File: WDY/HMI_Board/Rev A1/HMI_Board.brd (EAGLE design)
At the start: 128 x 31.5 mm, 30 parts, among them SW1 B3FS-1015, SW2 B3FS-1015, SW3 B3FS-1015, SW4 B3FS-1015, SW5 B3FS-1015, SW6 B3FS-1015, U1 90814-0208, U2 90814-0206

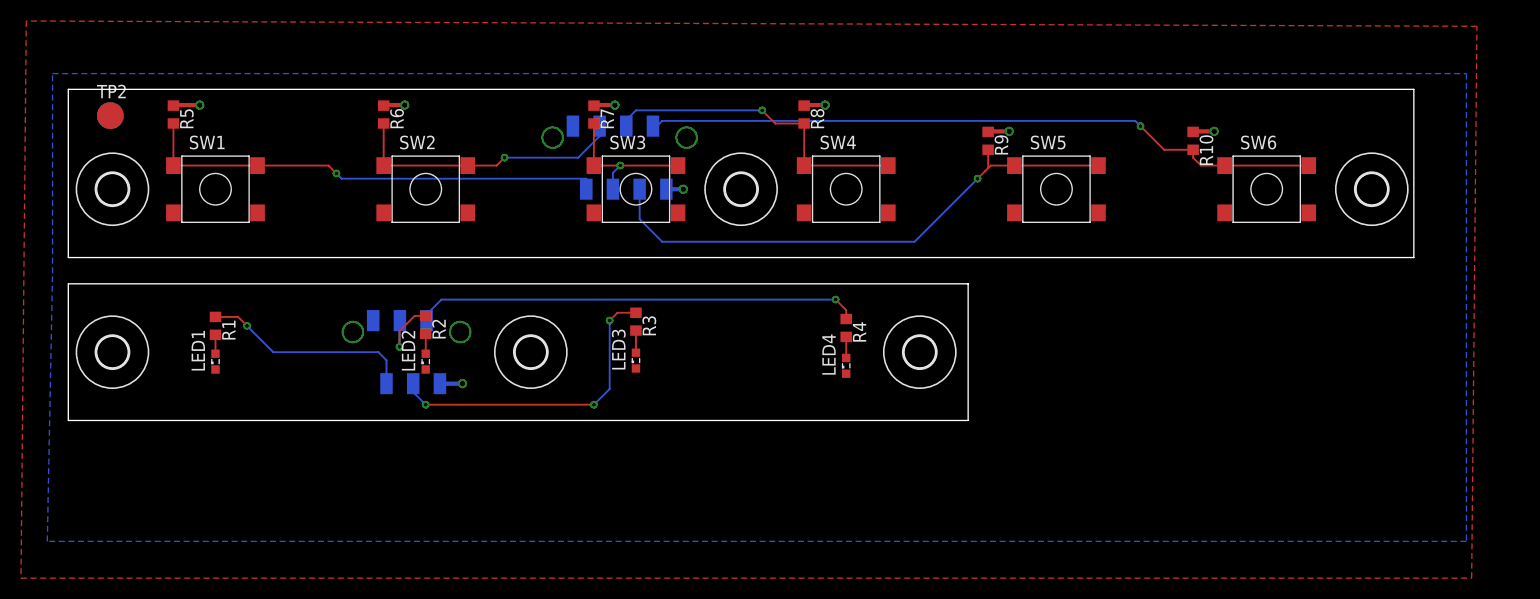
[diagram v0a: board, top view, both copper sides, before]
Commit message: Panelize the board, add fiducial
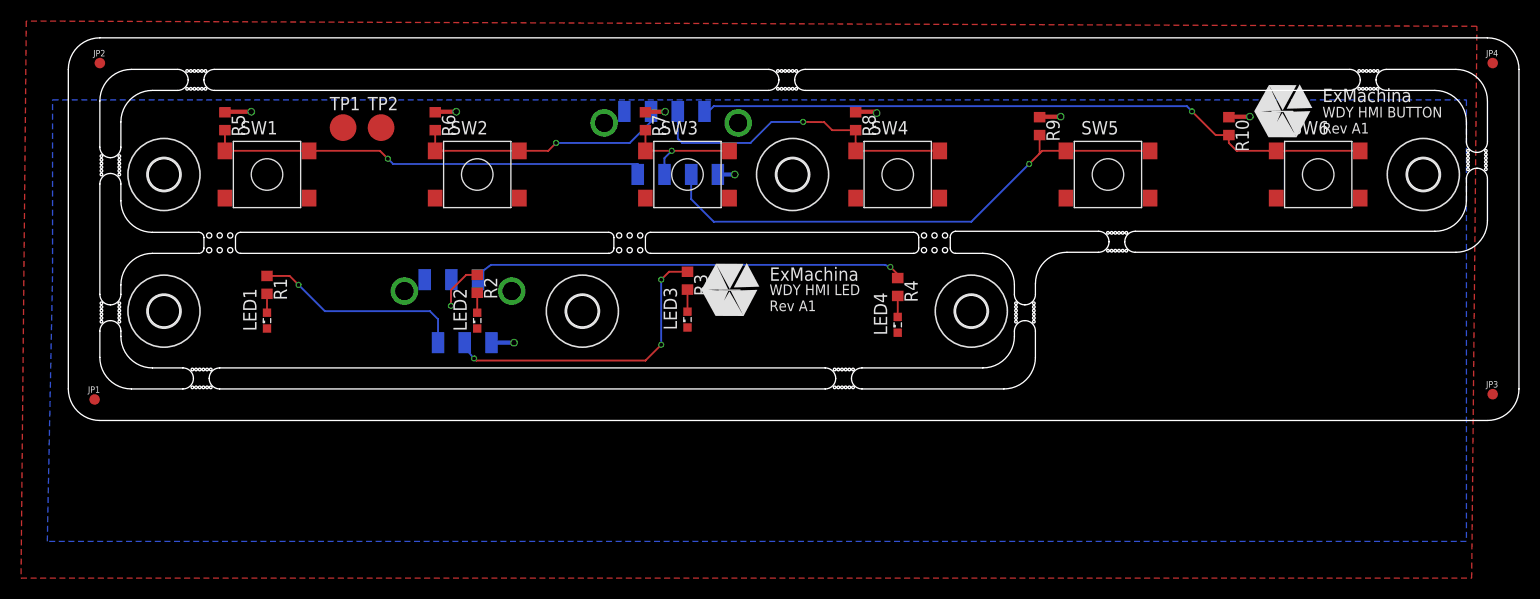
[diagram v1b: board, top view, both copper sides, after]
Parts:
- added JP1, JP2, JP3, JP4: FIDUCIAL1X2, SparkFun:FIDUCIAL-1X2
- added U$1, U$2: EXMACHINA-LOGO-NAME, exmachina:EXM-LOGO-BASELINE
- moved TP2 25.8 mm to (29.8, 27.9)
- moved TP1 22.2 mm to (26.1, 27.9), flipped to the top
- moved H4 6.26 mm to (85.9, 10.4)
- moved LED4 6.26 mm to (78.9, 9.10)
- moved R4 6.26 mm to (78.9, 12.7)
- moved H3 6.26 mm to (9.10, 10.4)
- moved H5 6.26 mm to (48.9, 10.4)
- moved LED1 6.26 mm to (18.9, 9.50)
- moved LED2 6.26 mm to (38.9, 9.50)
- moved R1 6.26 mm to (18.9, 12.9)
- moved R2 6.26 mm to (38.9, 13.0)
- moved R3 6.26 mm to (58.9, 13.3)
- moved U2 6.26 mm to (33.9, 13.4)
- moved LED3 6.26 mm to (58.9, 9.60)
- moved H1 5.10 mm to (128.9, 23.4)
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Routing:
- net HMI_BUTTON_2: track 26.7 -> 24.6 mm
- net HMI_BUTTON_1: track 44.8 -> 42.7 mm
- net HMI_BUTTON_3: track 14.5 -> 12.5 mm
- net HMI_BUTTON_4: track 30.4 -> 31.4 mm
- net HMI_LED_4: track 42.4 -> 41.4 mm
- net HMI_BUTTON_5: track 52.1 -> 51.4 mm
- net HMI_LED_3: track 29.9 -> 29.4 mm
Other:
- board size 128 x 31.5 mm -> 138 x 36.4 mm
- board text added: "WDY HMI BUTTON Rev A1"
- board text added: "WDY HMI LED Rev A1"

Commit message: Update libraries
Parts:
- moved TP2 6.48 mm to (23.4, 28.9)
- moved TP1 6.18 mm to (20.0, 28.9)
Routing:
- net +3V3: track 12.5 -> 15.7 mm
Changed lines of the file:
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@@
 <element name="H5" library="holes" package="3,0" value="MOUNT-HOLE3.0" x="48.9" y="10.4"/>
 <element name="H6" library="holes" package="3,0" value="MOUNT-HOLE3.0" x="9.1" y="23.4"/>
-<element name="TP1" library="testpad" package="B2,54" value="TPB2,54" x="26.14" y="27.86">
-<attribute name="TP_SIGNAL_NAME" value="" x="26.14" y="27.86" size="1.778" layer="27" display="off"/>
+<element name="TP1" library="testpad" package="B2,54" value="TPB2,54" x="20.04" y="28.86">
+<attribute name="TP_SIGNAL_NAME" value="" x="20.04" y="28.86" size="1.778" layer="27" display="off"/>
 </element>
-<element name="TP2" library="testpad" package="B2,54" value="TPB2,54" x="29.752" y="27.86">
-<attribute name="TP_SIGNAL_NAME" value="" x="29.752" y="27.86" size="1.778" layer="27" display="off"/>
+<element name="TP2" library="testpad" package="B2,54" value="TPB2,54" x="23.352" y="28.86">
+<attribute name="TP_SIGNAL_NAME" value="" x="23.352" y="28.86" size="1.778" layer="27" display="off"/>
 </element>
 <element name="U$1" library="exmachina" package="EXM-LOGO-BASELINE" value="EXMACHINA-LOGO-NAME" x="62.9" y="12.4"/>
@@
 <wire x1="40.2556" y1="7.4" x2="42.4" y2="7.4" width="0.4064" layer="16"/>
 <via x="42.4" y="7.4" extent="1-16" drill="0.5"/>
-<wire x1="58.9" y1="8.85" x2="54.9" y2="21.15" width="0" layer="19" extent="1-1"/>
+<wire x1="54.9" y1="21.15" x2="58.9" y2="8.85" width="0" layer="19" extent="1-1"/>
 </signal>
 <signal name="+3V3">
@@
 <wire x1="74.95" y1="29.368" x2="76.773" y2="29.368" width="0.4064" layer="1"/>
 <wire x1="76.773" y1="29.368" x2="76.9" y2="29.241" width="0.4064" layer="1"/>
-<wire x1="17.4" y1="29.368" x2="26.14" y2="27.86" width="0" layer="19" extent="1-1"/>
-<wire x1="52.9" y1="29.4" x2="54.9" y2="29.318" width="0" layer="19" extent="1-16"/>
-<wire x1="33.9" y1="13.4" x2="34.9" y2="29.318" width="0" layer="19" extent="1-16"/>
+<wire x1="17.4" y1="29.368" x2="20.04" y2="29.368" width="0.4064" layer="1"/>
+<wire x1="20.04" y1="29.368" x2="20.04" y2="28.86" width="0.4064" layer="1"/>
+<wire x1="34.9" y1="29.318" x2="33.9" y2="13.4" width="0" layer="19" extent="1-16"/>
 </signal>
 <signal name="HMI_LED_1" class="1">
@@
 <wire x1="34.9" y1="25.65" x2="34.9" y2="27.618" width="0.1778" layer="1"/>
 <wire x1="42.9" y1="25.65" x2="34.9" y2="25.65" width="0.1778" layer="1"/>
-<wire x1="42.9" y1="25.65" x2="45.65" y2="25.65" width="0.1778" layer="1"/>
-<wire x1="45.65" y1="25.65" x2="46.4" y2="26.4" width="0.1778" layer="1"/>
-<via x="46.4" y="26.4" extent="1-16" drill="0.35"/>
-<wire x1="46.4" y1="26.4" x2="53.4" y2="26.4" width="0.1778" layer="16"/>
-<wire x1="53.4" y1="26.4" x2="55.44" y2="28.44" width="0.1778" layer="16"/>
+<wire x1="42.9" y1="25.65" x2="46.15" y2="25.65" width="0.1778" layer="1"/>
+<wire x1="46.15" y1="25.65" x2="46.4" y2="25.9" width="0.1778" layer="1"/>
+<via x="46.4" y="25.9" extent="1-16" drill="0.35"/>
+<wire x1="46.4" y1="25.9" x2="52.9" y2="25.9" width="0.1778" layer="16"/>
+<wire x1="52.9" y1="25.9" x2="55.44" y2="28.44" width="0.1778" layer="16"/>
 <wire x1="55.44" y1="28.44" x2="55.44" y2="29.4" width="0.1778" layer="16"/>
 </signal>

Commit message: Add value on LED
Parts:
- LED1, LED2, LED3, LED4: value (none) -> Blue
- moved U1 5.41 mm to (57.4, 26.4)
- moved U2 3.91 mm to (36.9, 10.9)
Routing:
- net GND: track 3.76 -> 4.64 mm
- net HMI_LED_2: track 7.12 -> 7.79 mm
- net HMI_LED_3: track 29.4 -> 30.0 mm
- net HMI_LED_1: track 20.2 -> 19.5 mm
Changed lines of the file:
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@@
 </autorouter>
 <elements>
-<element name="LED1" library="led" package="SML0603" value="" x="18.9" y="9.5" rot="R90"/>
-<element name="LED2" library="led" package="SML0603" value="" x="38.9" y="9.5" rot="R90"/>
-<element name="LED3" library="led" package="SML0603" value="" x="58.9" y="9.6" rot="R90"/>
-<element name="LED4" library="led" package="SML0603" value="" x="78.9" y="9.1" rot="R90"/>
+<element name="LED1" library="led" package="SML0603" value="Blue" x="18.9" y="9.5" rot="R90"/>
+<element name="LED2" library="led" package="SML0603" value="Blue" x="38.9" y="9.5" rot="R90"/>
+<element name="LED3" library="led" package="SML0603" value="Blue" x="58.9" y="9.6" rot="R90"/>
+<element name="LED4" library="led" package="SML0603" value="Blue" x="78.9" y="9.1" rot="R90"/>
 <element name="R1" library="rcl" package="R0603" value="1k" x="18.9" y="12.9" rot="R270"/>
 <element name="R2" library="rcl" package="R0603" value="1k" x="38.9" y="13" rot="R270"/>
@@
 <element name="SW5" library="Switch_SMT" package="B3FS" value="B3FS-1015" x="98.9" y="23.4"/>
 <element name="R9" library="rcl" package="R0603" value="4k7" x="92.4" y="28" rot="R270"/>
-<element name="U1" library="Molex_By_element14_Batch_1" package="MOLEX_90814-0208" value="90814-0208" x="52.9" y="29.4" rot="MR180">
-<attribute name="SUPPLIER" value="Molex" x="52.9" y="29.4" size="1.778" layer="28" rot="MR180" display="off"/>
-<attribute name="MPN" value="90814-0208" x="52.9" y="29.4" size="1.778" layer="28" rot="MR180" display="off"/>
-<attribute name="OC_FARNELL" value="1757025" x="52.9" y="29.4" size="1.778" layer="28" rot="MR180" display="off"/>
-<attribute name="OC_NEWARK" value="34R6216" x="52.9" y="29.4" size="1.778" layer="28" rot="MR180" display="off"/>
-<attribute name="PACKAGE" value="CONN-8POS" x="52.9" y="29.4" size="1.778" layer="28" rot="MR180" display="off"/>
+<element name="U1" library="Molex_By_element14_Batch_1" package="MOLEX_90814-0208" value="90814-0208" x="57.4" y="26.4" rot="MR180">
+<attribute name="SUPPLIER" value="Molex" x="57.4" y="26.4" size="1.778" layer="28" rot="MR180" display="off"/>
+<attribute name="MPN" value="90814-0208" x="57.4" y="26.4" size="1.778" layer="28" rot="MR180" display="off"/>
+<attribute name="OC_FARNELL" value="1757025" x="57.4" y="26.4" size="1.778" layer="28" rot="MR180" display="off"/>
+<attribute name="OC_NEWARK" value="34R6216" x="57.4" y="26.4" size="1.778" layer="28" rot="MR180" display="off"/>
+<attribute name="PACKAGE" value="CONN-8POS" x="57.4" y="26.4" size="1.778" layer="28" rot="MR180" display="off"/>
 </element>
 <element name="SW6" library="Switch_SMT" package="B3FS" value="B3FS-1015" x="118.9" y="23.4"/>
 <element name="R10" library="rcl" package="R0603" value="4k7" x="110.4" y="28" rot="R270"/>
-<element name="U2" library="Molex_By_element14_Batch_1" package="MOLEX_90814-0206" value="90814-0206" x="33.9" y="13.4" rot="MR180">
-<attribute name="SUPPLIER" value="Molex" x="33.9" y="13.4" size="1.778" layer="28" rot="MR180" display="off"/>
-<attribute name="MPN" value="90814-0206" x="33.9" y="13.4" size="1.778" layer="28" rot="MR180" display="off"/>
-<attribute name="OC_FARNELL" value="1757024" x="33.9" y="13.4" size="1.778" layer="28" rot="MR180" display="off"/>
-<attribute name="OC_NEWARK" value="34R6215" x="33.9" y="13.4" size="1.778" layer="28" rot="MR180" display="off"/>
-<attribute name="PACKAGE" value="CONN-6 POS" x="33.9" y="13.4" size="1.778" layer="28" rot="MR180" display="off"/>
+<element name="U2" library="Molex_By_element14_Batch_1" package="MOLEX_90814-0206" value="90814-0206" x="36.9" y="10.9" rot="MR180">
+<attribute name="SUPPLIER" value="Molex" x="36.9" y="10.9" size="1.778" layer="28" rot="MR180" display="off"/>
+<attribute name="MPN" value="90814-0206" x="36.9" y="10.9" size="1.778" layer="28" rot="MR180" display="off"/>
+<attribute name="OC_FARNELL" value="1757024" x="36.9" y="10.9" size="1.778" layer="28" rot="MR180" display="off"/>
+<attribute name="OC_NEWARK" value="34R6215" x="36.9" y="10.9" size="1.778" layer="28" rot="MR180" display="off"/>
+<attribute name="PACKAGE" value="CONN-6 POS" x="36.9" y="10.9" size="1.778" layer="28" rot="MR180" display="off"/>
 </element>
 <element name="H1" library="holes" package="3,0" value="MOUNT-HOLE3.0" x="128.9" y="23.4"/>
@@
 <vertex x="133.5" y="-15"/>
 </polygon>
-<wire x1="61.79" y1="23.4056" x2="61.7956" y2="23.4" width="0.4064" layer="16"/>
+<wire x1="61.845" y1="23.5806" x2="61.7956" y2="23.4" width="0.4064" layer="16"/>
 <wire x1="61.7956" y1="23.4" x2="63.4" y2="23.4" width="0.4064" layer="16"/>
 <via x="63.4" y="23.4" extent="1-16" drill="0.5"/>
 <contactref element="TP2" pad="TP"/>
-<wire x1="40.25" y1="7.4056" x2="40.2556" y2="7.4" width="0.4064" layer="16"/>
+<wire x1="40.075" y1="8.0806" x2="40.2556" y2="7.4" width="0.4064" layer="16"/>
 <wire x1="40.2556" y1="7.4" x2="42.4" y2="7.4" width="0.4064" layer="16"/>
 <via x="42.4" y="7.4" extent="1-16" drill="0.5"/>
-<wire x1="54.9" y1="21.15" x2="58.9" y2="8.85" width="0" layer="19" extent="1-1"/>
+<wire x1="58.9" y1="8.85" x2="54.9" y2="21.15" width="0" layer="19" extent="1-1"/>
 </signal>
 <signal name="+3V3">
@@
 <wire x1="17.4" y1="29.368" x2="20.04" y2="29.368" width="0.4064" layer="1"/>
 <wire x1="20.04" y1="29.368" x2="20.04" y2="28.86" width="0.4064" layer="1"/>
-<wire x1="34.9" y1="29.318" x2="33.9" y2="13.4" width="0" layer="19" extent="1-16"/>
+<wire x1="33.725" y1="14.075" x2="34.9" y2="29.318" width="0" layer="19" extent="1-16"/>
 </signal>
 <signal name="HMI_LED_1" class="1">
@@
 <wire x1="24.4" y1="10.4" x2="34.4" y2="10.4" width="0.1778" layer="16"/>
 <wire x1="34.4" y1="10.4" x2="35.17" y2="9.63" width="0.1778" layer="16"/>
-<wire x1="35.17" y1="9.63" x2="35.17" y2="7.4056" width="0.1778" layer="16"/>
+<wire x1="35.17" y1="9.63" x2="34.995" y2="8.0806" width="0.1778" layer="16"/>
 </signal>
 <signal name="HMI_LED_2" class="1">
 <contactref element="R2" pad="1"/>
 <contactref element="U2" pad="3"/>
-<wire x1="36.44" y1="13.4" x2="36.4" y2="13.36" width="0.1778" layer="16"/>
+<wire x1="36.265" y1="14.075" x2="36.4" y2="13.36" width="0.1778" layer="16"/>
 <wire x1="36.4" y1="13.36" x2="36.4" y2="10.9" width="0.1778" layer="16"/>
 <via x="36.4" y="10.9" extent="1-16" drill="0.35"/>
@@
 <wire x1="38.6" y1="5.9" x2="37.9" y2="6.7" width="0.1778" layer="16"/>
 <wire x1="37.9" y1="6.7" x2="37.9" y2="7.2156" width="0.1778" layer="16"/>
-<wire x1="37.9" y1="7.2156" x2="37.71" y2="7.4056" width="0.1778" layer="16"/>
+<wire x1="37.9" y1="7.2156" x2="37.535" y2="8.0806" width="0.1778" layer="16"/>
 <via x="56.4" y="7.2" extent="1-16" drill="0.35"/>
 </signal>
@@
 <wire x1="78.9" y1="13.9" x2="78.9" y2="13.55" width="0.1778" layer="1"/>
 <wire x1="40.2" y1="14.8" x2="38.98" y2="13.88" width="0.1778" layer="16"/>
-<wire x1="38.98" y1="13.88" x2="38.98" y2="13.4" width="0.1778" layer="16"/>
+<wire x1="38.98" y1="13.88" x2="38.805" y2="14.075" width="0.1778" layer="16"/>
 </signal>
 <signal name="HMI_BUTTON_1" class="1">
@@
 <wire x1="30.4" y1="24.9" x2="30.9" y2="24.4" width="0.1778" layer="16"/>
 <wire x1="30.9" y1="24.4" x2="54.1644" y2="24.4" width="0.1778" layer="16"/>
-<wire x1="54.1644" y1="24.4" x2="54.17" y2="23.4056" width="0.1778" layer="16"/>
+<wire x1="54.1644" y1="24.4" x2="54.225" y2="23.5806" width="0.1778" layer="16"/>
 </signal>
 <signal name="HMI_BUTTON_2" class="1">
@@
 <wire x1="46.4" y1="25.9" x2="52.9" y2="25.9" width="0.1778" layer="16"/>
 <wire x1="52.9" y1="25.9" x2="55.44" y2="28.44" width="0.1778" layer="16"/>
-<wire x1="55.44" y1="28.44" x2="55.44" y2="29.4" width="0.1778" layer="16"/>
+<wire x1="55.44" y1="28.44" x2="55.495" y2="29.575" width="0.1778" layer="16"/>
 </signal>
 <signal name="HMI_BUTTON_3" class="1">
@@
 <wire x1="54.9" y1="27.618" x2="54.9" y2="25.65" width="0.1778" layer="1"/>
 <wire x1="54.9" y1="25.65" x2="57.4" y2="25.65" width="0.1778" layer="1"/>
-<wire x1="56.71" y1="23.4056" x2="56.71" y2="24.96" width="0.1778" layer="16"/>
+<wire x1="56.765" y1="23.5806" x2="56.71" y2="24.96" width="0.1778" layer="16"/>
 <wire x1="56.71" y1="24.96" x2="57.4" y2="25.65" width="0.1778" layer="16"/>
 <via x="57.4" y="25.65" extent="1-16" drill="0.35"/>
@@
 <wire x1="82.9" y1="25.65" x2="74.9" y2="25.65" width="0.1778" layer="1"/>
 <via x="69.9" y="28.4" extent="1-16" drill="0.35"/>
-<wire x1="57.98" y1="29.98" x2="57.98" y2="29.4" width="0.1778" layer="16"/>
+<wire x1="57.98" y1="29.98" x2="58.035" y2="29.575" width="0.1778" layer="16"/>
 <wire x1="74.9" y1="27.618" x2="72.662" y2="27.618" width="0.1778" layer="1"/>
 <wire x1="72.662" y1="27.618" x2="71.9" y2="28.38" width="0.1778" layer="1"/>
 <wire x1="71.9" y1="28.38" x2="69.9" y2="28.4" width="0.1778" layer="1"/>
-<wire x1="57.98" y1="29.4" x2="57.98" y2="26.82" width="0.1778" layer="16"/>
+<wire x1="58.035" y1="29.575" x2="57.98" y2="26.82" width="0.1778" layer="16"/>
 <wire x1="57.98" y1="26.82" x2="58.4" y2="26.4" width="0.1778" layer="16"/>
 <wire x1="58.4" y1="26.4" x2="64.892" y2="26.4" width="0.1778" layer="16"/>
@@
 <contactref element="U1" pad="6"/>
 <wire x1="102.9" y1="25.65" x2="94.9" y2="25.65" width="0.1778" layer="1"/>
-<wire x1="59.25" y1="23.4056" x2="59.25" y2="21.058" width="0.1778" layer="16"/>
+<wire x1="59.305" y1="23.5806" x2="59.25" y2="21.058" width="0.1778" layer="16"/>
 <wire x1="59.25" y1="21.058" x2="61.4" y2="18.908" width="0.1778" layer="16"/>
 <wire x1="61.4" y1="18.908" x2="85.908" y2="18.908" width="0.1778" layer="16"/>
@@
 <wire x1="109.15" y1="27.15" x2="110.4" y2="27.15" width="0.1778" layer="1"/>
 <wire x1="61.4" y1="29.9" x2="60.9" y2="29.4" width="0.1778" layer="16"/>
-<wire x1="60.9" y1="29.4" x2="60.52" y2="29.4" width="0.1778" layer="16"/>
+<wire x1="60.9" y1="29.4" x2="60.575" y2="29.575" width="0.1778" layer="16"/>
 </signal>
 </signals>
